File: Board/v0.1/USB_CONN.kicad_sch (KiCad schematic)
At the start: 6 parts, among them J2 USB_B_Micro

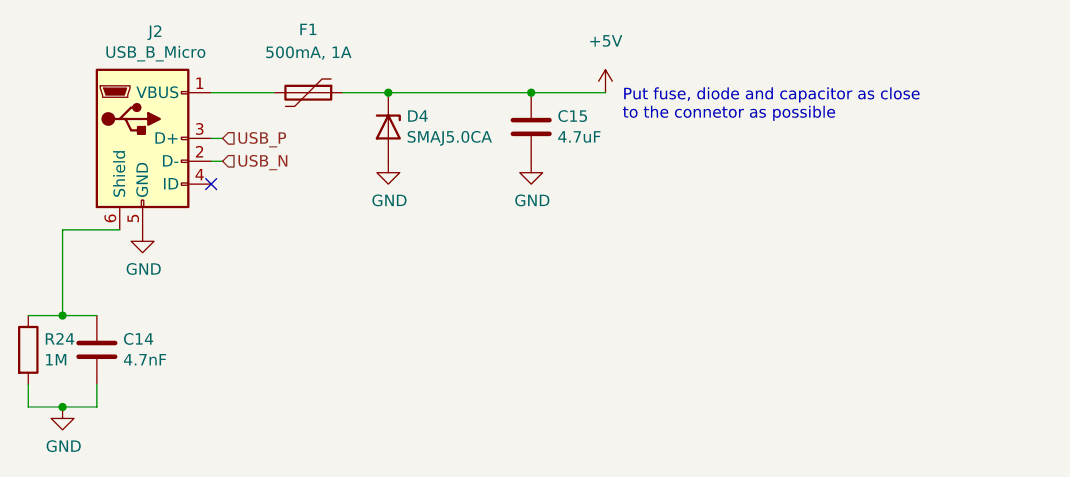
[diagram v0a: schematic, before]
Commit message: Fix missing pad for H1, fix missing power input ERC error
ERC error was: Input power pin not driven by any output power pins.
Fix was adding PWR_FLAG power symbol after polyfuse or inductor.
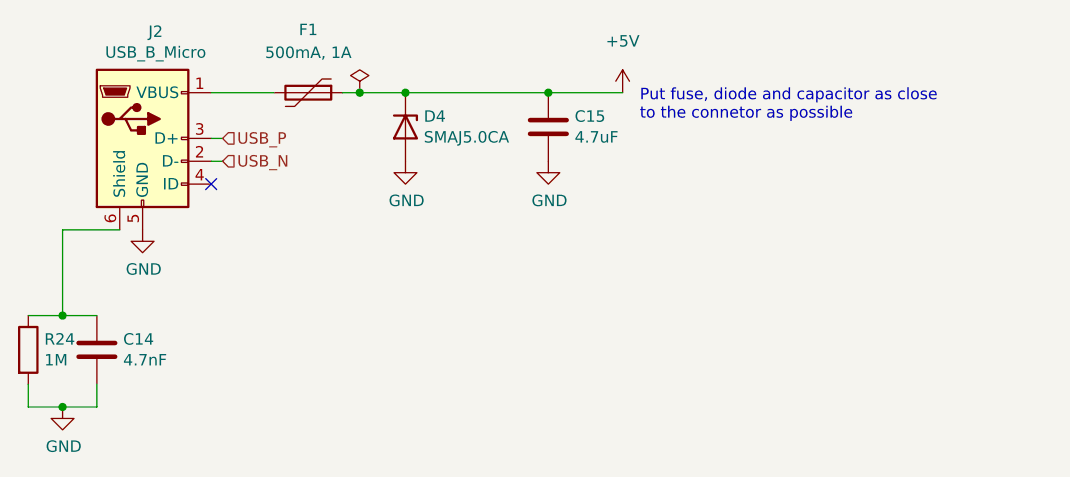
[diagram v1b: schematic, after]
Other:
- moved on the sheet: C15, D4
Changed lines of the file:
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@@
     (company "Bzgec")
   )
-  (junction (at 132.715 64.135) (diameter 0) (color 0 0 0 0)
+  (junction (at 134.62 64.135) (diameter 0) (color 0 0 0 0)
   )
   (junction (at 96.52 99.06) (diameter 0) (color 0 0 0 0)
   )
-  (junction (at 148.59 64.135) (diameter 0) (color 0 0 0 0)
+  (junction (at 150.495 64.135) (diameter 0) (color 0 0 0 0)
   )
   (junction (at 96.52 88.9) (diameter 0) (color 0 0 0 0)
+  )
+  (junction (at 129.54 64.135) (diameter 0) (color 0 0 0 0)
   )
   (no_connect (at 113.03 74.295))
@@
     (stroke (width 0) (type default) (color 0 0 0 0))
   )
-  (wire (pts (xy 148.59 64.135) (xy 156.845 64.135))
+  (wire (pts (xy 134.62 64.135) (xy 150.495 64.135))
+    (stroke (width 0) (type default) (color 0 0 0 0))
+  )
+  (wire (pts (xy 150.495 64.135) (xy 158.75 64.135))
     (stroke (width 0) (type default) (color 0 0 0 0))
   )
@@
     (stroke (width 0) (type default) (color 0 0 0 0))
   )
-  (wire (pts (xy 132.715 64.135) (xy 148.59 64.135))
-    (stroke (width 0) (type default) (color 0 0 0 0))
-  )
-  (wire (pts (xy 127.635 64.135) (xy 132.715 64.135))
+  (wire (pts (xy 129.54 64.135) (xy 134.62 64.135))
+    (stroke (width 0) (type default) (color 0 0 0 0))
+  )
+  (wire (pts (xy 127.635 64.135) (xy 129.54 64.135))
     (stroke (width 0) (type default) (color 0 0 0 0))
   )
@@
   )
   (text "Put fuse, diode and capacitor as close\nto the connetor as possible"
-    (at 158.75 67.31 0)
+    (at 160.655 67.31 0)
     (effects (font (size 1.27 1.27)) (justify left bottom))
   )
@@
     (pin "2")
   )
+  (symbol (lib_id "power:PWR_FLAG") (at 129.54 64.135 0) (unit 1)
+    (in_bom yes) (on_board yes)
+    (property "Reference" "#FLG0102" (id 0) (at 129.54 62.23 0)
+      (effects (font (size 1.27 1.27)) hide)
+    )
+    (property "Value" "PWR_FLAG" (id 1) (at 125.095 60.325 0)
+      (effects (font (size 1.27 1.27)) (justify left) hide)
+    )
+    (property "Footprint" "" (id 2) (at 129.54 64.135 0)
+      (effects (font (size 1.27 1.27)) hide)
+    )
+    (property "Datasheet" "~" (id 3) (at 129.54 64.135 0)
+      (effects (font (size 1.27 1.27)) hide)
+    )
+    (pin "1")
+  )
   (symbol (lib_id "Connector:USB_B_Micro") (at 105.41 69.215 0) (unit 1)
     (in_bom yes) (on_board yes)
@@
     (pin "6")
   )
-  (symbol (lib_id "power:+5V") (at 156.845 64.135 0) (unit 1)
+  (symbol (lib_id "power:+5V") (at 158.75 64.135 0) (unit 1)
     (in_bom yes) (on_board yes) (fields_autoplaced)
-    (property "Reference" "#PWR036" (id 0) (at 156.845 67.945 0)
-      (effects (font (size 1.27 1.27)) hide)
-    )
-    (property "Value" "+5V" (id 1) (at 156.845 58.42 0))
-    (property "Footprint" "" (id 2) (at 156.845 64.135 0)
-      (effects (font (size 1.27 1.27)) hide)
-    )
-    (property "Datasheet" "" (id 3) (at 156.845 64.135 0)
-      (effects (font (size 1.27 1.27)) hide)
-    )
-    (pin "1")
-  )
-  (symbol (lib_id "power:GND") (at 132.715 71.755 0) (unit 1)
-    (in_bom yes) (on_board yes)
-    (property "Reference" "#PWR034" (id 0) (at 132.715 78.105 0)
-      (effects (font (size 1.27 1.27)) hide)
-    )
-    (property "Value" "GND" (id 1) (at 132.842 76.1492 0))
-    (property "Footprint" "" (id 2) (at 132.715 71.755 0)
-      (effects (font (size 1.27 1.27)) hide)
-    )
-    (property "Datasheet" "" (id 3) (at 132.715 71.755 0)
-      (effects (font (size 1.27 1.27)) hide)
-    )
-    (pin "1")
-  )
-  (symbol (lib_id "power:GND") (at 148.59 71.755 0) (unit 1)
-    (in_bom yes) (on_board yes)
-    (property "Reference" "#PWR035" (id 0) (at 148.59 78.105 0)
-      (effects (font (size 1.27 1.27)) hide)
-    )
-    (property "Value" "GND" (id 1) (at 148.717 76.1492 0))
-    (property "Footprint" "" (id 2) (at 148.59 71.755 0)
-      (effects (font (size 1.27 1.27)) hide)
-    )
-    (property "Datasheet" "" (id 3) (at 148.59 71.755 0)
+    (property "Reference" "#PWR036" (id 0) (at 158.75 67.945 0)
+      (effects (font (size 1.27 1.27)) hide)
+    )
+    (property "Value" "+5V" (id 1) (at 158.75 58.42 0))
+    (property "Footprint" "" (id 2) (at 158.75 64.135 0)
+      (effects (font (size 1.27 1.27)) hide)
+    )
+    (property "Datasheet" "" (id 3) (at 158.75 64.135 0)
+      (effects (font (size 1.27 1.27)) hide)
+    )
+    (pin "1")
+  )
+  (symbol (lib_id "power:GND") (at 134.62 71.755 0) (unit 1)
+    (in_bom yes) (on_board yes)
+    (property "Reference" "#PWR034" (id 0) (at 134.62 78.105 0)
+      (effects (font (size 1.27 1.27)) hide)
+    )
+    (property "Value" "GND" (id 1) (at 134.747 76.1492 0))
+    (property "Footprint" "" (id 2) (at 134.62 71.755 0)
+      (effects (font (size 1.27 1.27)) hide)
+    )
+    (property "Datasheet" "" (id 3) (at 134.62 71.755 0)
+      (effects (font (size 1.27 1.27)) hide)
+    )
+    (pin "1")
+  )
+  (symbol (lib_id "power:GND") (at 150.495 71.755 0) (unit 1)
+    (in_bom yes) (on_board yes)
+    (property "Reference" "#PWR035" (id 0) (at 150.495 78.105 0)
+      (effects (font (size 1.27 1.27)) hide)
+    )
+    (property "Value" "GND" (id 1) (at 150.622 76.1492 0))
+    (property "Footprint" "" (id 2) (at 150.495 71.755 0)
+      (effects (font (size 1.27 1.27)) hide)
+    )
+    (property "Datasheet" "" (id 3) (at 150.495 71.755 0)
       (effects (font (size 1.27 1.27)) hide)
     )
@@
     (pin "2")
   )
-  (symbol (lib_id "Device:D_Zener") (at 132.715 67.945 270) (unit 1)
-    (in_bom yes) (on_board yes)
-    (property "Reference" "D4" (id 0) (at 134.747 66.7766 90)
-      (effects (font (size 1.27 1.27)) (justify left))
-    )
-    (property "Value" "SMAJ5.0CA" (id 1) (at 134.747 69.088 90)
-      (effects (font (size 1.27 1.27)) (justify left))
-    )
-    (property "Footprint" "Diode_SMD:D_SMA" (id 2) (at 132.715 67.945 0)
-      (effects (font (size 1.27 1.27)) hide)
-    )
-    (property "Datasheet" "https://www.littelfuse.com/~/media/electronics/datasheets/tvs_diodes/littelfuse_tvs_diode_smaj_datasheet.pdf.pdf" (id 3) (at 132.715 67.945 0)
-      (effects (font (size 1.27 1.27)) hide)
-    )
-    (pin "1")
-    (pin "2")
-  )
-  (symbol (lib_id "Device:C") (at 148.59 67.945 0) (unit 1)
-    (in_bom yes) (on_board yes)
-    (property "Reference" "C15" (id 0) (at 151.511 66.7766 0)
-      (effects (font (size 1.27 1.27)) (justify left))
-    )
-    (property "Value" "4.7uF" (id 1) (at 151.511 69.088 0)
-      (effects (font (size 1.27 1.27)) (justify left))
-    )
-    (property "Footprint" "Capacitor_SMD:C_0603_1608Metric_Pad1.08x0.95mm_HandSolder" (id 2) (at 149.5552 71.755 0)
-      (effects (font (size 1.27 1.27)) hide)
-    )
-    (property "Datasheet" "~" (id 3) (at 148.59 67.945 0)
-      (effects (font (size 1.27 1.27)) hide)
-    )
+  (symbol (lib_id "Device:D_Zener") (at 134.62 67.945 270) (unit 1)
+    (in_bom yes) (on_board yes)
+    (property "Reference" "D4" (id 0) (at 136.652 66.7766 90)
+      (effects (font (size 1.27 1.27)) (justify left))
+    )
+    (property "Value" "SMAJ5.0CA" (id 1) (at 136.652 69.088 90)
+      (effects (font (size 1.27 1.27)) (justify left))
+    )
+    (property "Footprint" "Diode_SMD:D_SMA" (id 2) (at 134.62 67.945 0)
+      (effects (font (size 1.27 1.27)) hide)
+    )
+    (property "Datasheet" "https://www.littelfuse.com/~/media/electronics/datasheets/tvs_diodes/littelfuse_tvs_diode_smaj_datasheet.pdf.pdf" (id 3) (at 134.62 67.945 0)
+      (effects (font (size 1.27 1.27)) hide)
+    )
+    (pin "1")
+    (pin "2")
+  )
+  (symbol (lib_id "Device:C") (at 150.495 67.945 0) (unit 1)
+    (in_bom yes) (on_board yes)
+    (property "Reference" "C15" (id 0) (at 153.416 66.7766 0)
+      (effects (font (size 1.27 1.27)) (justify left))
+    )
+    (property "Value" "4.7uF" (id 1) (at 153.416 69.088 0)
+      (effects (font (size 1.27 1.27)) (justify left))
+    )
+    (property "Footprint" "Capacitor_SMD:C_0603_1608Metric_Pad1.08x0.95mm_HandSolder" (id 2) (at 151.4602 71.755 0)
+      (effects (font (size 1.27 1.27)) hide)
+    )
+    (property "Datasheet" "~" (id 3) (at 150.495 67.945 0)
+      (effects (font (size 1.27 1.27)) hide)
+    )
